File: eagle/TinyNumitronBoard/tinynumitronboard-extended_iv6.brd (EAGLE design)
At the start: 100 x 50 mm, 37 parts

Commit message: Post 2nd script exec, all look ok
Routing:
- net N$105: track 45.0 -> 0.00 mm, vias 2 -> 0
- net N$53: track 0.00 -> 44.9 mm, vias 0 -> 2
- net N$99: track 34.2 -> 0.00 mm, vias 2 -> 0
- net N$63: track 0.00 -> 34.2 mm, vias 0 -> 2
- net N$82: track 19.7 -> 0.00 mm
- net N$58: track 0.00 -> 19.7 mm
- net N$64: track 0.00 -> 10.8 mm
- net N$87: track 10.8 -> 0.00 mm
- net N$54: track 0.00 -> 9.51 mm
- net N$81: track 9.49 -> 0.00 mm
- net N$60: track 0.00 -> 9.22 mm, vias 0 -> 1
- net N$84: track 9.20 -> 0.00 mm, vias 1 -> 0
- net N$62: track 0.00 -> 9.07 mm
- net N$86: track 9.05 -> 0.00 mm
- net N$94: track 8.15 -> 0.00 mm, vias 1 -> 0
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
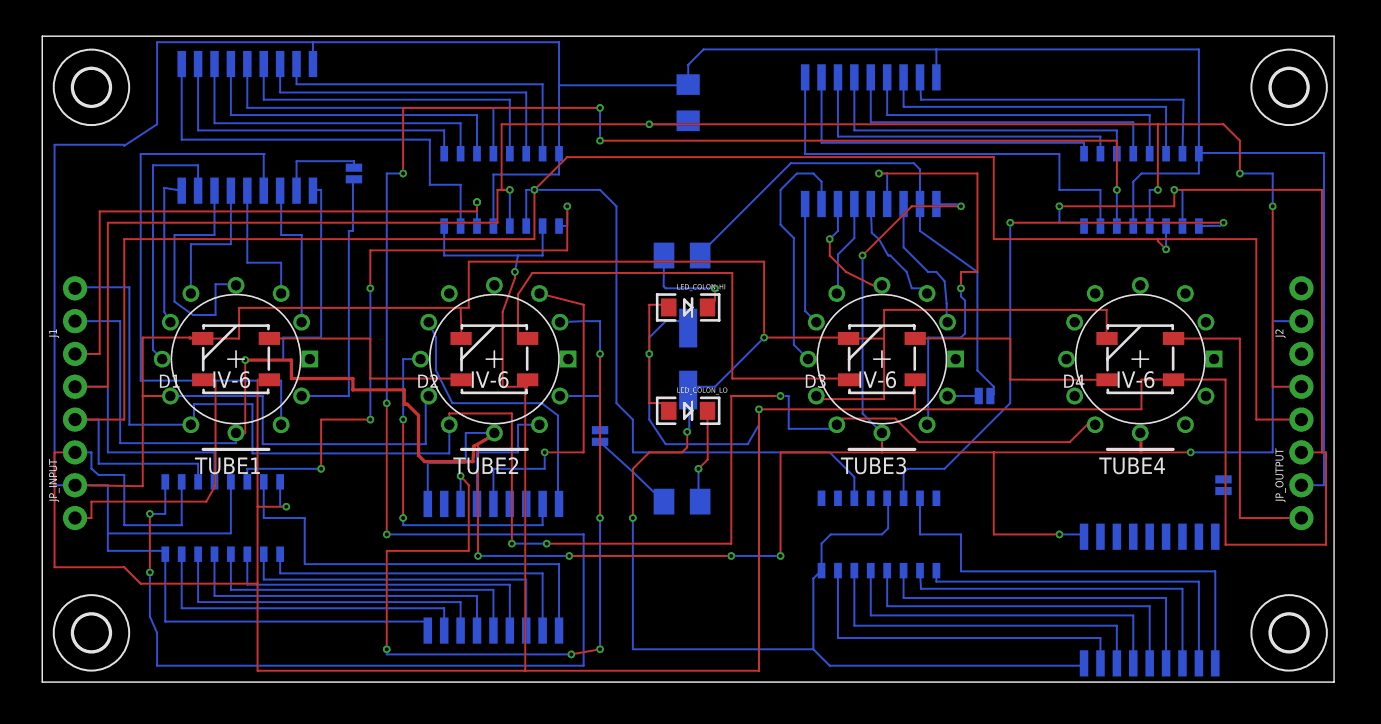
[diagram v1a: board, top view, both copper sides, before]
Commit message: Wiring continued (95%)
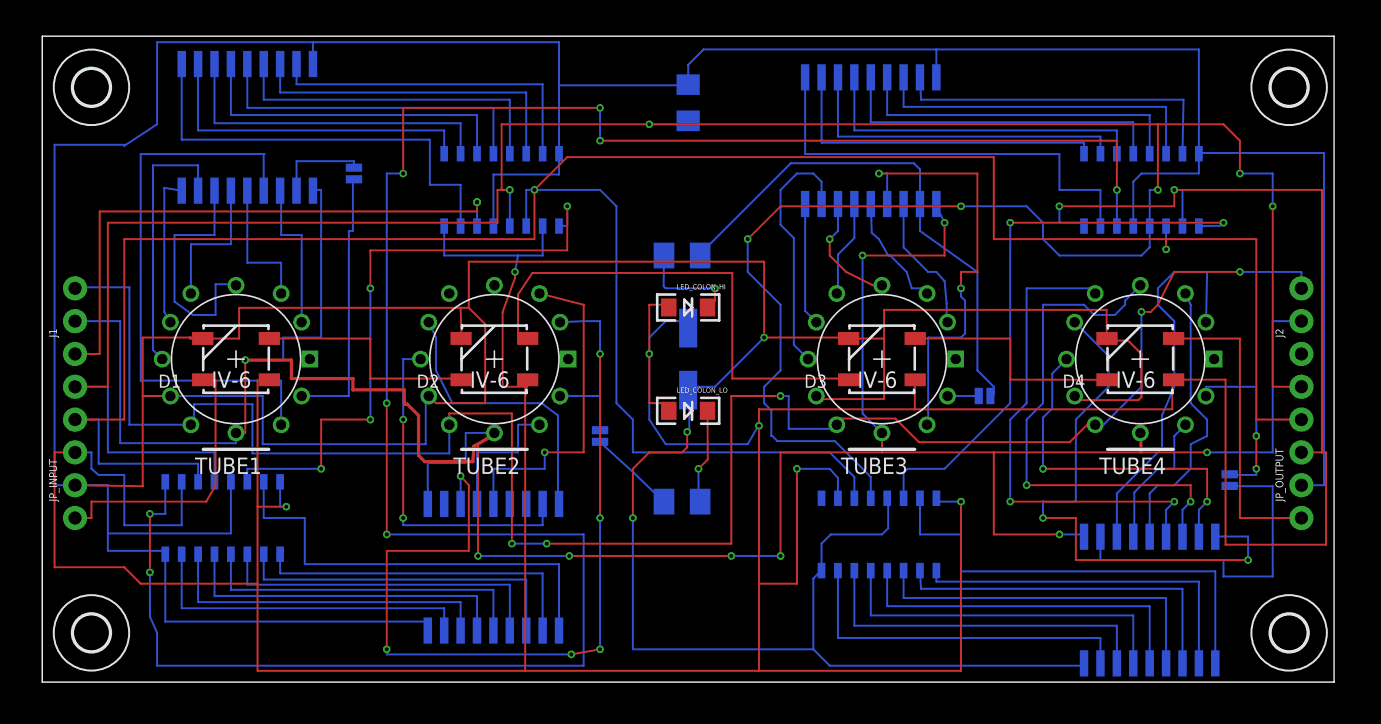
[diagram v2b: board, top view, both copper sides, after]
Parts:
- moved JP_DOT_TUBE4 0.62 mm to (91.9, 15.6)
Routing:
- net RCK: track 169.0 -> 233.0 mm, vias 5 -> 7
- net VCC: track 330.2 -> 376.7 mm, vias 6 -> 8
- net N$97: track 0.00 -> 43.4 mm, vias 0 -> 2
- net N$90: track 0.00 -> 40.4 mm, vias 0 -> 2
- net N$82: track 0.00 -> 38.3 mm, vias 0 -> 2
- net N$85: track 0.00 -> 29.6 mm
- net N$93: track 0.00 -> 27.5 mm, vias 0 -> 2
- net N$83: track 0.00 -> 26.7 mm
- net FIL_P: track 0.00 -> 26.0 mm, vias 0 -> 2
- net GND: track 463.1 -> 487.6 mm
- net N$81: track 0.00 -> 22.3 mm
- net N$78: track 0.00 -> 13.5 mm, vias 0 -> 2
- net N$84: track 0.00 -> 11.1 mm
- net N$89: track 25.5 -> 24.8 mm

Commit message: Wiring continued (99%)
And where I noticed that semi-colon LEDS won't work
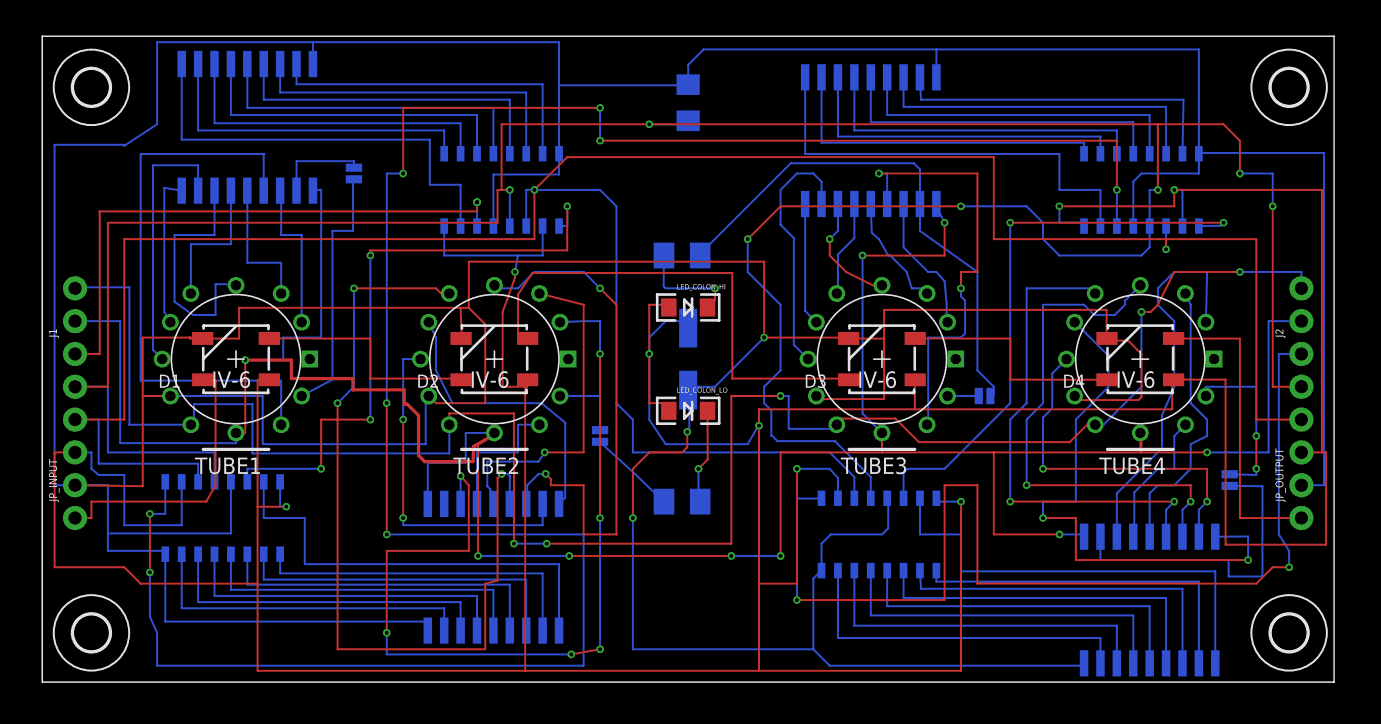
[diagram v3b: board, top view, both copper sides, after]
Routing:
- net N$107: track 0.00 -> 83.4 mm, vias 0 -> 2
- net N$21: track 0.00 -> 64.8 mm, vias 0 -> 3
- net FIL_P: track 26.0 -> 73.3 mm
- net N$124: track 47.1 -> 0.00 mm
- net N$24: track 0.00 -> 43.4 mm, vias 0 -> 2
- net N$97: track 43.4 -> 0.00 mm, vias 2 -> 0
- net N$26: track 0.00 -> 40.4 mm, vias 0 -> 2
- net N$90: track 40.4 -> 0.00 mm, vias 2 -> 0
- net N$82: track 38.3 -> 0.00 mm, vias 2 -> 0
- net N$27: track 0.00 -> 38.2 mm, vias 0 -> 2
- net N$30: track 0.00 -> 29.6 mm
- net N$85: track 29.6 -> 0.00 mm
- net N$25: track 0.00 -> 27.5 mm, vias 0 -> 2
- net N$93: track 27.5 -> 0.00 mm, vias 2 -> 0
- net N$31: track 0.00 -> 25.1 mm
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
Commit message: Removed LEDs for colon
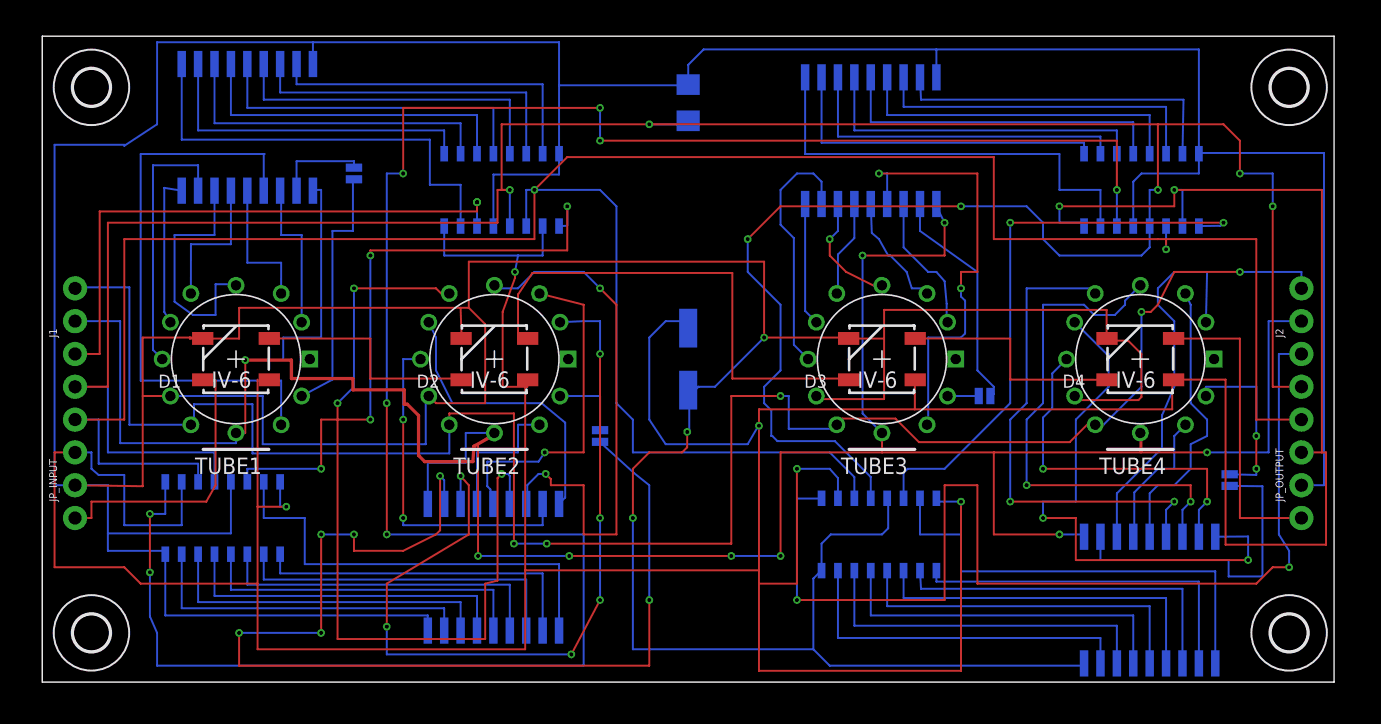
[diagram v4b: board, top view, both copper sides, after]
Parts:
- removed LED_COLON_HI, LED_COLON_LO: (no value), SparkFun-LED:LED-1206
- removed R_COLON_HI, R_COLON_LO: 470, resistor:M1206
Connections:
- removed net N$22: LED_COLON_LO.C, R_COLON_LO.2
- removed net N$77: LED_COLON_HI.C, R_COLON_HI.2
- net N$43: no longer R_COLON_LO.1
- net N$65: no longer R_COLON_HI.1
- net VCC: no longer LED_COLON_HI.A, LED_COLON_LO.A
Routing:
- net FIL_P: track 73.3 -> 128.5 mm, vias 2 -> 5
- net N$20: track 55.2 -> 84.7 mm, vias 3 -> 6
- net N$88: track 40.9 -> 17.7 mm
- net N$125: track 22.7 -> 0.00 mm
- net GRID_P: track 164.0 -> 186.7 mm
- net VCC: track 376.7 -> 362.4 mm, vias 8 -> 7
- net N$77: track 8.15 -> 0.00 mm, vias 1 -> 0
- net N$22: track 7.40 -> 0.00 mm, vias 1 -> 0
- net N$159: track 6.74 -> 0.00 mm
- net N$42: track 67.6 -> 63.5 mm
- net N$21: track 64.8 -> 63.2 mm

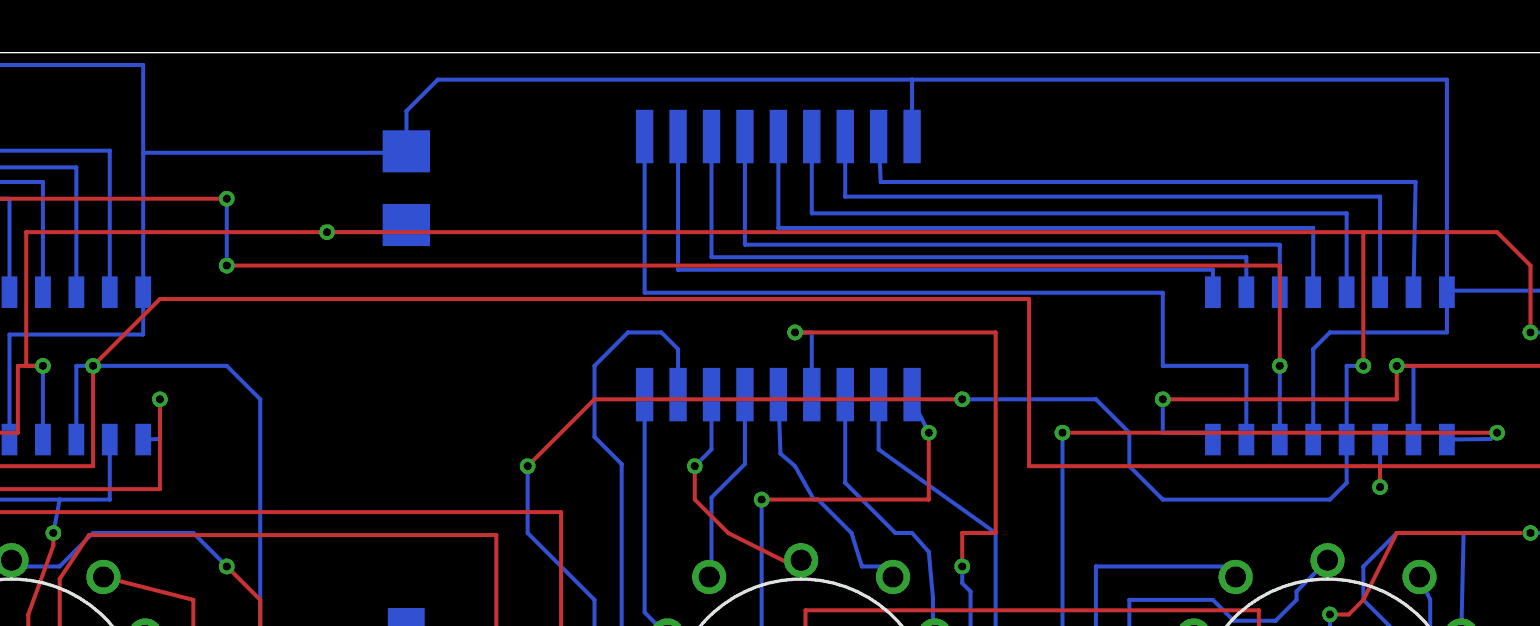
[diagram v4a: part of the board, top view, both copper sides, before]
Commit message: Added cap for CLK
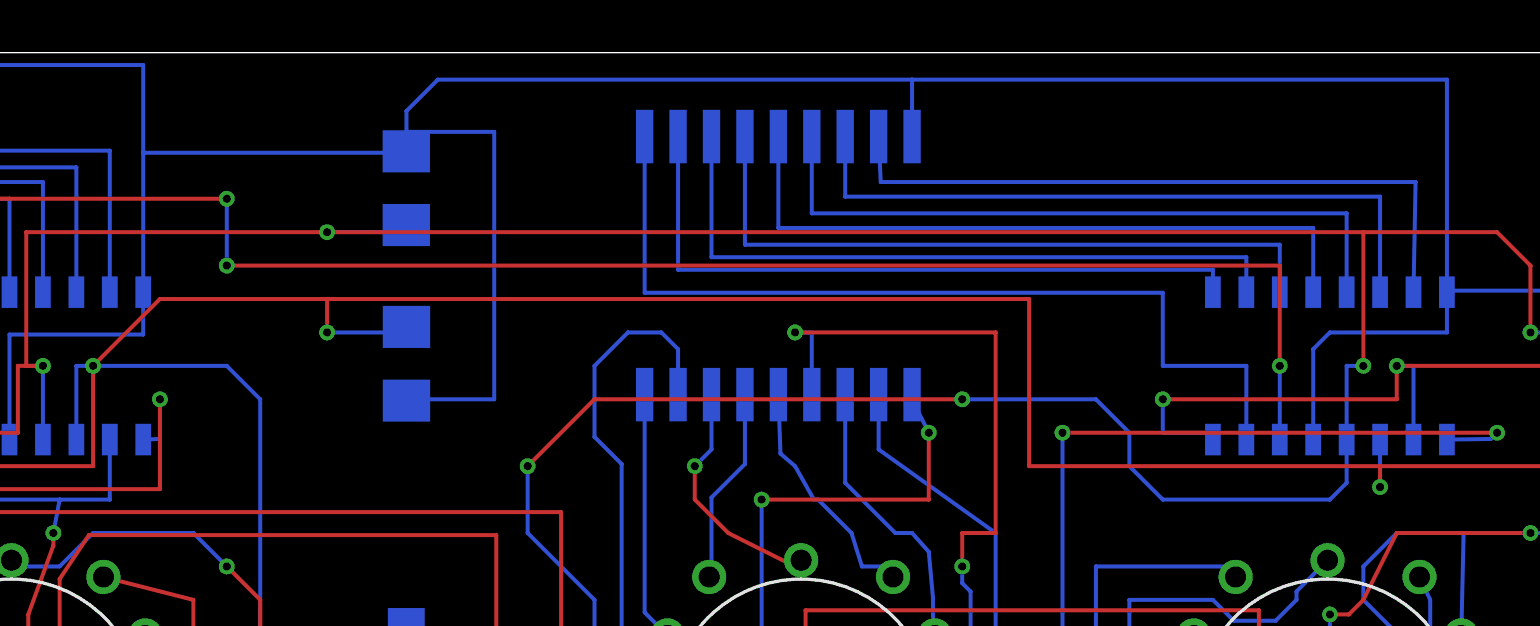
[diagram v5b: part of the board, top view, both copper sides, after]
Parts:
- added C3: 1uF, resistor:C1206
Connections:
- net GND: now also C3.2
- net SCK: now also C3.1
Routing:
- net GND: track 487.6 -> 504.5 mm
- net SCK: track 200.6 -> 205.0 mm, vias 2 -> 3
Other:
- board text added: "C1 1uF (Ltch)"
- board text added: "C3 1uF (CLK)"
- board text removed: "C1 1uF"
- board text removed: "R_Colon_Hi 470"
- board text removed: "R_Colon_Lo 470"
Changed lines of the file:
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@@
 <wire x1="52.07" y1="3.81" x2="50.8" y2="2.54" width="0.1524" layer="52"/>
 <text x="49.8475" y="4.445" size="1.27" layer="52" font="vector" rot="MR0">Front</text>
-<text x="53.6575" y="43.815" size="1.016" layer="52" font="vector" rot="MR0">C1
-1uF</text>
+<text x="53.81625" y="41.036875" size="1.016" layer="52" font="vector" rot="MR0">C1
+1uF
+(Ltch)</text>
 <text x="7.3025" y="12.065" size="1.27" layer="52" font="vector" rot="MR0">LED</text>
 <text x="8.5725" y="27.305" size="1.27" layer="52" font="vector" rot="MR0">+Grid</text>
@@
 <text x="68.2625" y="24.765" size="1.27" layer="52" font="vector" rot="MR0">[Tube 3]</text>
 <text x="88.5825" y="24.765" size="1.27" layer="52" font="vector" rot="MR0">[Tube 4]</text>
-<text x="56.03875" y="33.49625" size="1.016" layer="52" font="vector" rot="MR0">R_Colon_Hi
-470</text>
-<text x="55.324375" y="9.763125" size="1.016" layer="52" font="vector" rot="MR0">R_Colon_Lo
-470</text>
 <text x="40.3225" y="37.465" size="1.27" layer="52" font="vector" rot="MR0">74xx595</text>
 <text x="17.4625" y="12.065" size="1.27" layer="52" font="vector" rot="MR0">74xx595</text>
@@
 <text x="89.8525" y="3.175" size="1.27" layer="52" font="vector" rot="MR0">[Tube 4]</text>
 <text x="78.74" y="7.14375" size="1.27" layer="52" font="vector" rot="MR0">[Tube 4]</text>
+<text x="53.895625" y="34.210625" size="1.016" layer="52" font="vector" rot="MR0">C3
+1uF
+(CLK)</text>
 </plain>
 <attributes>
@@
 <element name="J1" library="SparkFun-Connectors" package="1X02_NO_SILK" value="" x="2.54" y="27.94" rot="R90"/>
 <element name="J2" library="SparkFun-Connectors" package="1X02_NO_SILK" value="" x="97.4725" y="27.94" rot="R90"/>
+<element name="C3" library="resistor" package="C1206" value="1uF" x="50.00625" y="38.179375" rot="MR270"/>
 </elements>
 <signals>
@@
 <wire x1="50.8" y1="22.86" x2="50.244375" y2="22.86" width="0.1524" layer="16"/>
 <wire x1="50.244375" y1="22.86" x2="50.00625" y2="22.621875" width="0.1524" layer="16"/>
-<wire x1="50.00625" y1="46.19625" x2="50.00625" y2="47.78375" width="0.1524" layer="16"/>
+<wire x1="50.00625" y1="46.19625" x2="50.00625" y2="46.99" width="0.1524" layer="16"/>
+<wire x1="50.00625" y1="46.99" x2="50.00625" y2="47.78375" width="0.1524" layer="16"/>
 <wire x1="50.00625" y1="47.78375" x2="51.196875" y2="48.974375" width="0.1524" layer="16"/>
 <wire x1="51.196875" y1="48.974375" x2="69.215" y2="48.974375" width="0.1524" layer="16"/>
@@
 <wire x1="30.48" y1="21.59" x2="29.924375" y2="22.145625" width="0.1524" layer="1"/>
 <wire x1="34.29" y1="27.701875" x2="33.02" y2="28.971875" width="0.1524" layer="1"/>
+<contactref element="C3" pad="2"/>
+<wire x1="50.00625" y1="36.750625" x2="50.8" y2="36.83" width="0.1524" layer="16"/>
+<wire x1="50.8" y1="36.83" x2="53.34" y2="36.83" width="0.1524" layer="16"/>
+<wire x1="53.34" y1="36.83" x2="53.34" y2="46.99" width="0.1524" layer="16"/>
+<wire x1="53.34" y1="46.99" x2="50.00625" y2="46.99" width="0.1524" layer="16"/>
 <wire x1="89.535" y1="40.9575" x2="89.535" y2="40.9" width="0" layer="19" extent="16-16"/>
 <wire x1="84.455" y1="35.3" x2="84.455" y2="35.321875" width="0" layer="19" extent="16-16"/>
@@
 <wire x1="9.92" y1="22.1425" x2="9.921875" y2="22.145625" width="0" layer="19" extent="1-1"/>
 <wire x1="62.423" y1="26.6" x2="62.38875" y2="26.590625" width="0" layer="19" extent="1-1"/>
+<wire x1="50.00625" y1="36.779375" x2="50.00625" y2="36.750625" width="0" layer="19" extent="16-16"/>
 <wire x1="62.468125" y1="26.590625" x2="62.423" y2="26.6" width="0" layer="19" extent="1-1"/>
 <wire x1="79.92" y1="22.1425" x2="79.930625" y2="22.145625" width="0" layer="19" extent="1-1"/>
@@
 <wire x1="62.865" y1="15.875" x2="62.865" y2="14.208125" width="0.1524" layer="16"/>
 <wire x1="38.1" y1="38.1" x2="40.64" y2="40.64" width="0.1524" layer="1"/>
-<wire x1="40.64" y1="40.64" x2="73.66" y2="40.64" width="0.1524" layer="1"/>
+<wire x1="40.64" y1="40.64" x2="46.99" y2="40.64" width="0.1524" layer="1"/>
+<wire x1="46.99" y1="40.64" x2="73.66" y2="40.64" width="0.1524" layer="1"/>
 <wire x1="73.66" y1="40.64" x2="73.66" y2="34.29" width="0.1524" layer="1"/>
-<wire x1="73.66" y1="34.29" x2="86.36" y2="34.29" width="0.1524" layer="1"/>
+<wire x1="73.66" y1="34.29" x2="86.995" y2="34.29" width="0.1524" layer="1"/>
 <wire x1="86.995" y1="34.29" x2="86.995" y2="33.49625" width="0.1524" layer="1"/>
 <wire x1="86.995" y1="33.49625" x2="86.995" y2="35.321875" width="0.1524" layer="16"/>
 <via x="86.995" y="33.49625" extent="1-16" drill="0.3048"/>
-<wire x1="86.36" y1="34.29" x2="86.995" y2="34.29" width="0.1524" layer="1"/>
 <wire x1="86.995" y1="34.29" x2="93.98" y2="34.29" width="0.1524" layer="1"/>
 <wire x1="93.98" y1="34.29" x2="93.98" y2="20.32" width="0.1524" layer="1"/>
 <wire x1="93.98" y1="20.32" x2="97.4725" y2="20.32" width="0.1524" layer="1"/>
+<contactref element="C3" pad="1"/>
+<wire x1="46.99" y1="40.64" x2="46.99" y2="39.37" width="0.1524" layer="1"/>
+<wire x1="46.99" y1="39.37" x2="49.53" y2="39.37" width="0.1524" layer="16"/>
+<wire x1="49.53" y1="39.37" x2="50.00625" y2="39.608125" width="0.1524" layer="16"/>
+<via x="46.99" y="39.37" extent="1-16" drill="0.3048"/>
 <wire x1="86.995" y1="35.321875" x2="86.995" y2="35.3" width="0" layer="19" extent="16-16"/>
 <wire x1="62.865" y1="14.23" x2="62.865" y2="14.208125" width="0" layer="19" extent="16-16"/>
 <wire x1="12.065" y1="15.5" x2="12.065" y2="15.478125" width="0" layer="19" extent="16-16"/>
+<wire x1="50.00625" y1="39.579375" x2="50.00625" y2="39.608125" width="0" layer="19" extent="16-16"/>
 <wire x1="37.465" y1="35.3" x2="37.465" y2="35.2425" width="0" layer="19" extent="16-16"/>
 </signal>
